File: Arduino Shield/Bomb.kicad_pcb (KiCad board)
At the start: 2 copper layers, 27.9 x 21.6 mm, 5 parts, among them J1 Digital/PWM, J2 I2C Out, J3 Power, J4 Logic, U1 ATtiny85

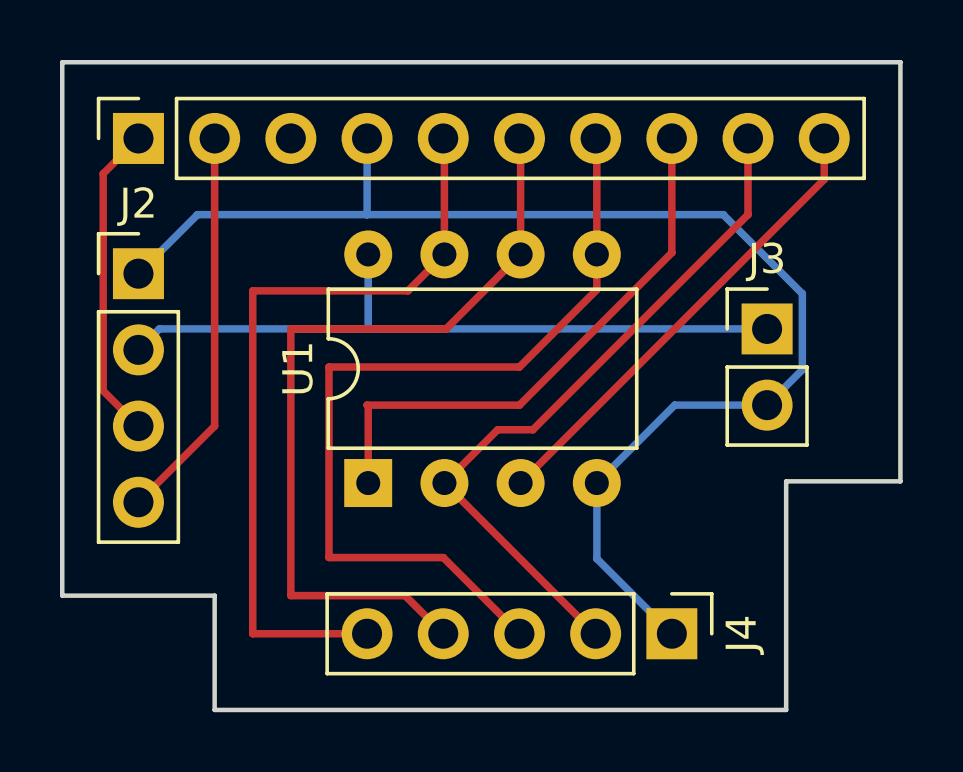
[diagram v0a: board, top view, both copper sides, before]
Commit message: Added markings near the GND and 5V, added capacitor between 5V and GND, generated fabrication files
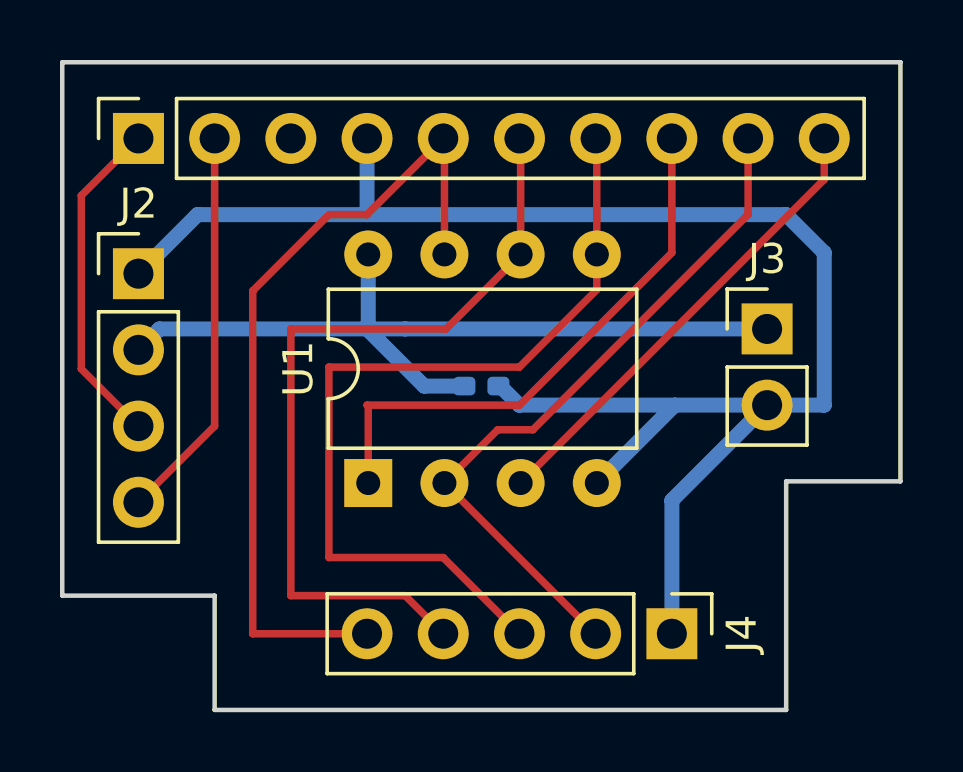
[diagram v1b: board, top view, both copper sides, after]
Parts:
- added C1: C, Capacitor_SMD:C_0402_1005Metric_Pad0.74x0.62mm_HandSolder, B.Cu at (129.2, 57.5)
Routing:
- net GND: track 43.6 -> 55.5 mm
- net +5V: track 23.7 -> 27.7 mm
- net /13: track 26.0 -> 27.6 mm
- net /SCL/A5: track 10.6 -> 11.2 mm
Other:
- board text added: "+"
- board text added: "-"
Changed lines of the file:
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@@
     (grid_origin 115.24 46.66)
     (pcbplotparams
-      (layerselection 0x0000030_80000001)
+      (layerselection 0x00010fc_ffffffff)
       (disableapertmacros false)
-      (usegerberextensions false)
+      (usegerberextensions true)
       (usegerberattributes true)
       (usegerberadvancedattributes true)
-      (creategerberjobfile true)
+      (creategerberjobfile false)
       (svguseinch false)
       (svgprecision 6)
@@
       (psa4output false)
       (plotreference true)
-      (plotvalue true)
+      (plotvalue false)
       (plotinvisibletext false)
       (sketchpadsonfab false)
-      (subtractmaskfromsilk false)
+      (subtractmaskfromsilk true)
       (outputformat 1)
       (mirror false)
-      (drillshape 1)
+      (drillshape 0)
       (scaleselection 1)
-      (outputdirectory "")
+      (outputdirectory "Gerber/")
     )
   )
@@
       (effects (font (size 1 1) (thickness 0.15)))
     )
-    (fp_text value "Power" (at 2.638165 1.27 90) (layer "F.Fab")
+    (fp_text value "Power" (at 2.638165 1.27 90) (layer "F.Fab") hide
       (effects (font (size 1 1) (thickness 0.15)))
     )
@@
     )
   )
+  (footprint "Capacitor_SMD:C_0402_1005Metric_Pad0.74x0.62mm_HandSolder" (layer "B.Cu")
+    (at 129.21 57.455)
+    (descr "Capacitor SMD 0402 (1005 Metric), square (rectangular) end terminal, IPC_7351 nominal with elongated pad for handsoldering. (Body size source: IPC-SM-782 page 76, https://www.pcb-3d.com/wordpress/wp-content/uploads/ipc-sm-782a_amendment_1_and_2.pdf), generated with kicad-footprint-generator")
+    (tags "capacitor handsolder")
+    (property "Sheetfile" "Bomb.kicad_sch")
+    (property "Sheetname" "")
+    (attr smd)
+    (fp_text reference "C1" (at 0 1.16 180) (layer "B.SilkS")
+      (effects (font (size 1 1) (thickness 0.15)) (justify mirror))
+    )
+    (fp_text value "C" (at 0 -1.16 180) (layer "B.Fab") hide
+      (effects (font (size 1 1) (thickness 0.15)) (justify mirror))
+    )
+    (fp_text user "${REFERENCE}" (at 0 0 180) (layer "B.Fab")
+      (effects (font (size 0.25 0.25) (thickness 0.04)) (justify mirror))
+    )
+    (fp_line (start -0.115835 0.36) (end 0.115835 0.36) (layer "B.SilkS") (width 0.12))
+    (fp_line (start -0.115835 -0.36) (end 0.115835 -0.36) (layer "B.SilkS") (width 0.12))
+    (fp_line (start -1.08 -0.46) (end -1.08 0.46) (layer "B.CrtYd") (width 0.05))
+    (fp_line (start 1.08 0.46) (end 1.08 -0.46) (layer "B.CrtYd") (width 0.05))
+    (fp_line (start 1.08 -0.46) (end -1.08 -0.46) (layer "B.CrtYd") (width 0.05))
+    (fp_line (start -1.08 0.46) (end 1.08 0.46) (layer "B.CrtYd") (width 0.05))
+    (fp_line (start -0.5 0.25) (end 0.5 0.25) (layer "B.Fab") (width 0.1))
+    (fp_line (start 0.5 0.25) (end 0.5 -0.25) (layer "B.Fab") (width 0.1))
+    (fp_line (start 0.5 -0.25) (end -0.5 -0.25) (layer "B.Fab") (width 0.1))
+    (fp_line (start -0.5 -0.25) (end -0.5 0.25) (layer "B.Fab") (width 0.1))
+    (pad "1" smd roundrect (at -0.5675 0) (size 0.735 0.62) (layers "B.Cu" "B.Paste" "B.Mask") (roundrect_rratio 0.25)
+      (net 2 "+5V") (pintype "passive"))
+    (pad "2" smd roundrect (at 0.5675 0) (size 0.735 0.62) (layers "B.Cu" "B.Paste" "B.Mask") (roundrect_rratio 0.25)
+      (net 1 "GND") (pintype "passive"))
+    (model "${KICAD6_3DMODEL_DIR}/Capacitor_SMD.3dshapes/C_0402_1005Metric.wrl"
+      (offset (xyz 0 0 0))
+      (scale (xyz 1 1 1))
+      (rotate (xyz 0 0 0))
+    )
+  )
   (gr_line (start 115.24 64.44) (end 115.24 46.66) (layer "Edge.Cuts") (width 0.15))
   (gr_line (start 120.32 64.44) (end 120.32 68.25) (layer "Edge.Cuts") (width 0.15))
@@
   (gr_line (start 115.24 46.66) (end 143.18 46.66) (layer "Edge.Cuts") (width 0.15))
   (gr_line (start 139.37 60.63) (end 143.18 60.63) (layer "Edge.Cuts") (width 0.15))
-  (segment (start 133.059261 63.209261) (end 135.56 65.71) (width 0.25) (layer "B.Cu") (net 1))
-  (segment (start 138.735 58.09) (end 139.91 56.915) (width 0.25) (layer "B.Cu") (net 1))
-  (segment (start 119.7475 51.74) (end 117.78 53.7075) (width 0.25) (layer "B.Cu") (net 1))
-  (segment (start 125.4 51.74) (end 119.7475 51.74) (width 0.25) (layer "B.Cu") (net 1))
-  (segment (start 133.059261 60.686243) (end 133.059261 63.209261) (width 0.25) (layer "B.Cu") (net 1))
-  (segment (start 125.4 51.74) (end 125.4 49.2) (width 0.25) (layer "B.Cu") (net 1))
-  (segment (start 139.91 54.375) (end 137.275 51.74) (width 0.25) (layer "B.Cu") (net 1))
-  (segment (start 137.275 51.74) (end 125.4 51.74) (width 0.25) (layer "B.Cu") (net 1))
-  (segment (start 135.655504 58.09) (end 133.059261 60.686243) (width 0.25) (layer "B.Cu") (net 1))
-  (segment (start 139.91 56.915) (end 139.91 54.375) (width 0.25) (layer "B.Cu") (net 1))
-  (segment (start 138.735 58.09) (end 135.655504 58.09) (width 0.25) (layer "B.Cu") (net 1))
-  (segment (start 125.4 55.55) (end 118.4775 55.55) (width 0.25) (layer "B.Cu") (net 2))
-  (segment (start 126.67 55.55) (end 125.4 55.55) (width 0.25) (layer "B.Cu") (net 2))
-  (segment (start 125.439261 53.066243) (end 125.439261 55.510739) (width 0.25) (layer "B.Cu") (net 2))
-  (segment (start 118.4775 55.55) (end 117.78 56.2475) (width 0.25) (layer "B.Cu") (net 2))
-  (segment (start 138.735 55.55) (end 126.67 55.55) (width 0.25) (layer "B.Cu") (net 2))
+  (gr_text "-" (at 135.56 63.17 90) (layer "F.Fab")
+    (effects (font (size 1 1) (thickness 0.15)))
+  )
+  (gr_text "-" (at 140.64 58.09 -270) (layer "F.Fab")
+    (effects (font (size 1 1) (thickness 0.15)))
+  )
+  (gr_text "+" (at 140.64 55.55 -270) (layer "F.Fab")
+    (effects (font (size 1 1) (thickness 0.15)))
+  )
+  (segment (start 140.64 58.09) (end 138.735 58.09) (width 0.5) (layer "B.Cu") (net 1))
+  (segment (start 139.37 51.74) (end 140.64 53.01) (width 0.5) (layer "B.Cu") (net 1))
+  (segment (start 119.7475 51.74) (end 117.78 53.7075) (width 0.5) (layer "B.Cu") (net 1))
+  (segment (start 135.56 61.265) (end 135.56 65.71) (width 0.5) (layer "B.Cu") (net 1))
+  (segment (start 130.4725 58.09) (end 129.8375 57.455) (width 0.5) (layer "B.Cu") (net 1))
+  (segment (start 138.735 58.09) (end 135.56 61.265) (width 0.5) (layer "B.Cu") (net 1))
+  (segment (start 125.4 51.74) (end 119.7475 51.74) (width 0.5) (layer "B.Cu") (net 1))
+  (segment (start 125.4 51.74) (end 139.37 51.74) (width 0.5) (layer "B.Cu") (net 1))
+  (segment (start 125.4 51.74) (end 125.4 49.2) (width 0.5) (layer "B.Cu") (net 1))
+  (segment (start 135.655504 58.09) (end 130.4725 58.09) (width 0.5) (layer "B.Cu") (net 1))
+  (segment (start 140.64 53.01) (end 140.64 58.09) (width 0.5) (layer "B.Cu") (net 1))
+  (segment (start 135.655504 58.09) (end 133.059261 60.686243) (width 0.5) (layer "B.Cu") (net 1))
+  (segment (start 138.735 58.09) (end 135.655504 58.09) (width 0.5) (layer "B.Cu") (net 1))
+  (segment (start 125.4 55.55) (end 118.4775 55.55) (width 0.5) (layer "B.Cu") (net 2))
+  (segment (start 138.735 55.55) (end 126.67 55.55) (width 0.5) (layer "B.Cu") (net 2))
+  (segment (start 127.305 57.455) (end 128.5825 57.455) (width 0.5) (layer "B.Cu") (net 2))
+  (segment (start 125.439261 53.066243) (end 125.439261 55.510739) (width 0.5) (layer "B.Cu") (net 2))
+  (segment (start 125.4 55.55) (end 127.305 57.455) (width 0.5) (layer "B.Cu") (net 2))
+  (segment (start 118.4775 55.55) (end 117.78 56.2475) (width 0.5) (layer "B.Cu") (net 2))
+  (segment (start 125.439261 55.510739) (end 125.478522 55.55) (width 0.25) (layer "B.Cu") (net 2))
   (segment (start 125.439261 55.510739) (end 125.4 55.55) (width 0.25) (layer "B.Cu") (net 2))
+  (segment (start 125.478522 55.55) (end 126.67 55.55) (width 0.5) (layer "B.Cu") (net 2))
   (segment (start 120.32 49.2) (end 120.32 58.7875) (width 0.25) (layer "F.Cu") (net 3))
   (segment (start 120.32 58.7875) (end 117.78 61.3275) (width 0.25) (layer "F.Cu") (net 3))
-  (segment (start 117.78 49.2) (end 116.605 50.375) (width 0.25) (layer "F.Cu") (net 4))
-  (segment (start 116.605 50.375) (end 116.605 57.6125) (width 0.25) (layer "F.Cu") (net 4))
-  (segment (start 116.605 57.6125) (end 117.78 58.7875) (width 0.25) (layer "F.Cu") (net 4))
+  (segment (start 117.78 49.2) (end 115.875 51.105) (width 0.25) (layer "F.Cu") (net 4))
+  (segment (start 115.875 56.8825) (end 117.78 58.7875) (width 0.25) (layer "F.Cu") (net 4))
+  (segment (start 115.875 51.105) (end 115.875 56.8825) (width 0.25) (layer "F.Cu") (net 4))
+  (segment (start 125.4 51.74) (end 124.13 51.74) (width 0.25) (layer "F.Cu") (net 5))
   (segment (start 121.59 65.71) (end 125.4 65.71) (width 0.25) (layer "F.Cu") (net 5))
-  (segment (start 126.765504 54.28) (end 121.59 54.28) (width 0.25) (layer "F.Cu") (net 5))
   (segment (start 127.979261 49.239261) (end 127.94 49.2) (width 0.25) (layer "F.Cu") (net 5))
-  (segment (start 127.979261 53.066243) (end 126.765504 54.28) (width 0.25) (layer "F.Cu") (net 5))
+  (segment (start 124.13 51.74) (end 121.59 54.28) (width 0.25) (layer "F.Cu") (net 5))
+  (segment (start 127.94 49.2) (end 125.4 51.74) (width 0.25) (layer "F.Cu") (net 5))
   (segment (start 121.59 54.28) (end 121.59 65.71) (width 0.25) (layer "F.Cu") (net 5))
   (segment (start 127.979261 53.066243) (end 127.979261 49.239261) (width 0.25) (layer "F.Cu") (net 5))
